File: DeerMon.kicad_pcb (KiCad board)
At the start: 4 copper layers, 30 x 45 mm, 62 parts, among them J1 TYPE-C-31-M-12, J2 ZJY144S025, J3 GPIO, M1 Mark, M2 Mark, M3 Mark, M4 Mark, P1 Position, P2 Position, P3 Position, P4 Position, P5 Position, Q1 DDC114TH, Q2 2N7002, SW1 BOOT, SW2 EN, U1 CP2102N-A02-GQFN24R, U2 AW9364DNR, U3 SPX3819M5-L-3-3, U4 ESP32-PICO-V3-02

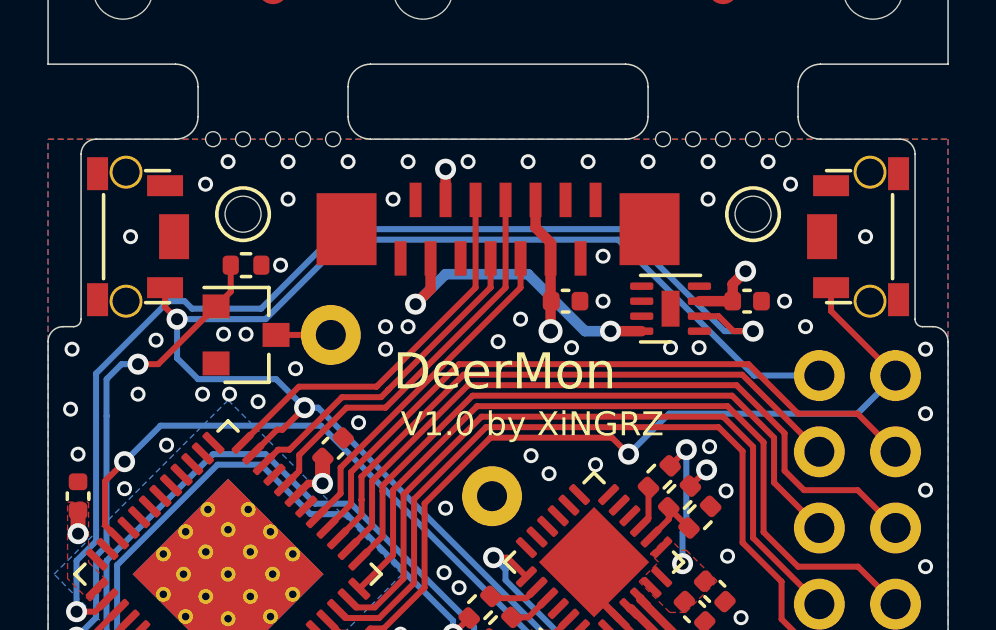
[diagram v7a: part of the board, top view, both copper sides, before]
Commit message: Update silks
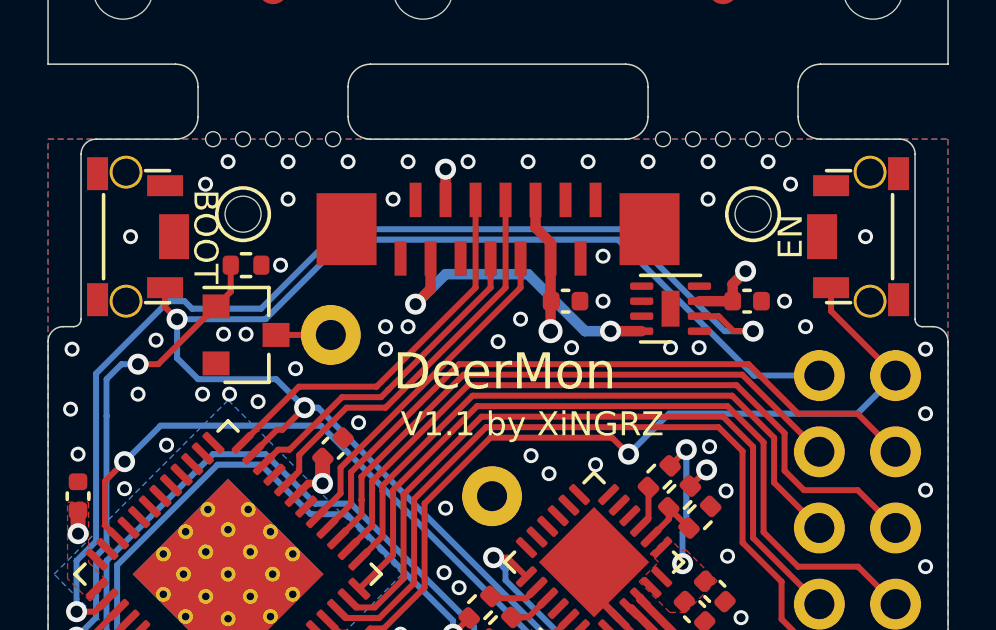
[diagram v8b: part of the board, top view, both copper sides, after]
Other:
- board text added: "BOOT"
- board text added: "BOOT 26 33 35 5 G TX"
- board text added: "EN"
- board text added: "EN 27 25 32 34 G RX G G"
- board text added: "V1.1 by XiNGRZ"
- board text removed: "BOOT 26 33 35 5 22 TX"
- board text removed: "EN 27 25 32 34 19 RX G G"
- board text removed: "V1.0 by XiNGRZ"
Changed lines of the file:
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@@
   (general
     (thickness 1.6)
-    (drawings 96)
+    (drawings 100)
     (tracks 581)
     (zones 0)
@@
     )
   )
+  (gr_text BOOT (at 52 53.3 90) (layer B.SilkS)
+    (effects (font (size 0.8 0.8) (thickness 0.12)) (justify mirror))
+  )
+  (gr_text EN (at 78 53.25 270) (layer B.SilkS)
+    (effects (font (size 0.8 0.8) (thickness 0.12)) (justify mirror))
+  )
+  (gr_text BOOT (at 55.25 53.25 270) (layer F.SilkS)
+    (effects (font (size 0.8 0.8) (thickness 0.12)))
+  )
+  (gr_text EN (at 74.75 53.25 90) (layer F.SilkS)
+    (effects (font (size 0.8 0.8) (thickness 0.12)))
+  )
   (gr_circle (center 71.75 78) (end 72.75 78) (layer Margin) (width 0.15))
   (gr_text JLCJLCJLCJLC (at 65 85) (layer F.SilkS)
@@
   (gr_arc (start 50.85 56) (end 50.85 56.25) (angle -90) (layer Edge.Cuts) (width 0.05))
   (gr_line (start 51.1 50.5) (end 51.1 56) (layer Edge.Cuts) (width 0.05))
-  (gr_text "BOOT\n\n26\n\n33\n\n35\n\n5\n\n22\n\nTX\n\n \n\n " (at 72.5 68.05) (layer B.SilkS)
+  (gr_text "BOOT\n\n26\n\n33\n\n35\n\n5\n\nG\n\nTX\n\n \n\n " (at 72.5 68.05) (layer B.SilkS)
     (effects (font (size 0.77 0.7) (thickness 0.12)) (justify left mirror))
   )
-  (gr_text "EN\n\n27\n\n25\n\n32\n\n34\n\n19\n\nRX\n\nG\n\nG" (at 74.2 68.05) (layer B.SilkS)
+  (gr_text "EN\n\n27\n\n25\n\n32\n\n34\n\nG\n\nRX\n\nG\n\nG" (at 74.2 68.05) (layer B.SilkS)
     (effects (font (size 0.77 0.7) (thickness 0.12)) (justify left mirror))
   )
-  (gr_text "V1.0 by XiNGRZ" (at 61.75 59.5) (layer F.SilkS)
+  (gr_text "V1.1 by XiNGRZ" (at 61.75 59.5) (layer F.SilkS)
     (effects (font (size 0.8 0.8) (thickness 0.12)) (justify left))
   )
